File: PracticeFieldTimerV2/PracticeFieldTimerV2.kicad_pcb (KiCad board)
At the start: 2 copper layers, 106 x 153.7 mm, 43 parts, among them J1 External Controls, J3 Panel, J5 /CAN Enable, J6 RJ45-B, J7 RJ45-A, J8 CAN Terminate, U1 ESP32-DevKitC, U2 PCF8574N, U3 20 x 4 LCD, U4 DS3231MZ_TRL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

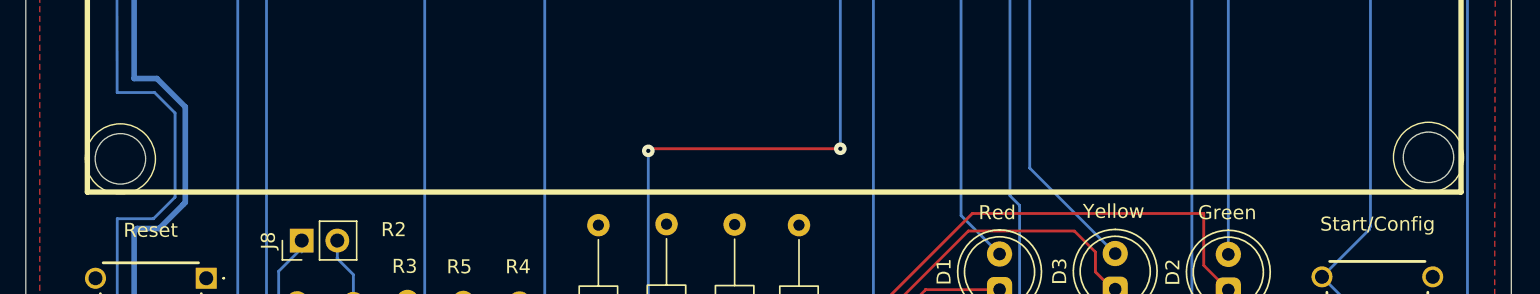
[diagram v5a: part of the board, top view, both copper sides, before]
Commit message: Clean up LCD mounting holes.
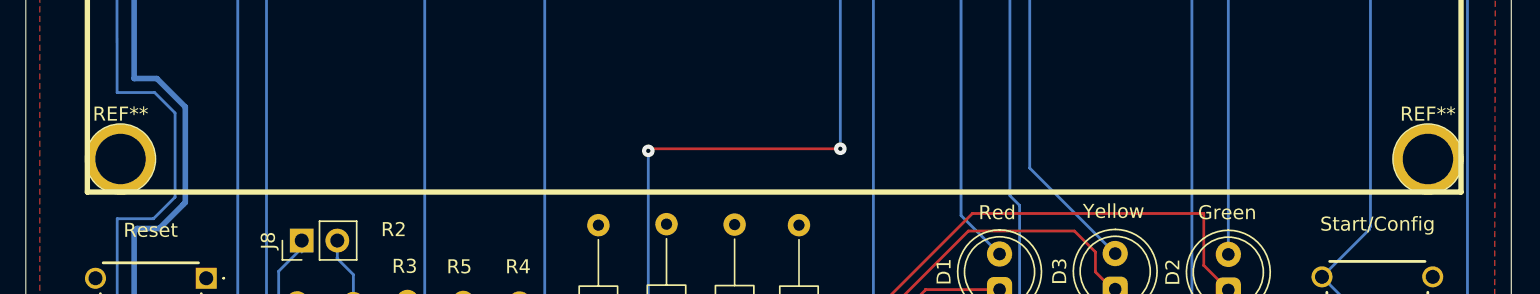
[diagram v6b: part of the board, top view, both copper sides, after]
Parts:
- removed the REF** at (140.1, 119.6)
- removed the REF** at (46.8, 119.7)
- added REF**: Untitled, Misc:M3-Hole-With-2.5mm-Radius-Boundary, F.Cu at (140.0, 119.7)
- added REF**: Untitled, Misc:M3-Hole-With-2.5mm-Radius-Boundary, F.Cu at (46.8, 119.7)
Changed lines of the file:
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@@
 		(embedded_fonts no)
 	)
-	(footprint "Misc:M3_HoleWith2.5mmRing"
-		(layer "F.Cu")
-		(at 140.07 119.57)
-		(property "Reference" "REF**"
-			(at 0 -3.6 0)
-			(unlocked yes)
-			(layer "F.SilkS")
-			(hide yes)
-			(effects
-				(font
-					(size 1 1)
-					(thickness 0.1)
-				)
-			)
-		)
-		(property "Value" "M3_2.5mm_Offset"
-			(at 0 4.2 0)
-			(unlocked yes)
-			(layer "F.Fab")
-			(effects
-				(font
-					(size 1 1)
-					(thickness 0.15)
-				)
-			)
-		)
-		(property "Datasheet" ""
-			(at 0 0 0)
-			(unlocked yes)
-			(layer "F.Fab")
-			(hide yes)
-			(effects
-				(font
-					(size 1 1)
-					(thickness 0.15)
-				)
-			)
-		)
-		(property "Description" "M3 Mounting Hole With 2.5 mm Ring"
-			(at 0 0 0)
-			(unlocked yes)
-			(layer "F.Fab")
-			(hide yes)
-			(effects
-				(font
-					(size 1 1)
-					(thickness 0.15)
-				)
-			)
-		)
-		(attr through_hole)
-		(fp_circle
-			(center 0 0)
-			(end 2.5 0)
-			(stroke
-				(width 0.1)
-				(type solid)
-			)
-			(fill no)
-			(layer "F.SilkS")
-		)
-		(fp_circle
-			(center 0 0)
-			(end 1.8 0)
-			(stroke
-				(width 0.05)
-				(type solid)
-			)
-			(fill no)
-			(layer "Edge.Cuts")
-		)
-		(embedded_fonts no)
-	)
 	(footprint "Misc:SW_500ASSP1M2QE"
 		(locked yes)
@@
 		)
 	)
+	(footprint "Misc:M3-Hole-With-2.5mm-Radius-Boundary"
+		(layer "F.Cu")
+		(at 140.03 119.69)
+		(property "Reference" "REF**"
+			(at 0 -3.2 0)
+			(unlocked yes)
+			(layer "F.SilkS")
+			(effects
+				(font
+					(size 1 1)
+					(thickness 0.1)
+				)
+			)
+		)
+		(property "Value" "Untitled"
+			(at 0 3.3 0)
+			(unlocked yes)
+			(layer "F.Fab")
+			(effects
+				(font
+					(size 1 1)
+					(thickness 0.15)
+				)
+			)
+		)
+		(property "Datasheet" ""
+			(at 0 0 0)
+			(unlocked yes)
+			(layer "F.Fab")
+			(hide yes)
+			(effects
+				(font
+					(size 1 1)
+					(thickness 0.15)
+				)
+			)
+		)
+		(property "Description" ""
+			(at 0 0 0)
+			(unlocked yes)
+			(layer "F.Fab")
+			(hide yes)
+			(effects
+				(font
+					(size 1 1)
+					(thickness 0.15)
+				)
+			)
+		)
+		(attr through_hole)
+		(fp_circle
+			(center 0 0)
+			(end 0 -2.5)
+			(stroke
+				(width 0.1)
+				(type default)
+			)
+			(fill no)
+			(layer "F.SilkS")
+		)
+		(fp_text user "${REFERENCE}"
+			(at 0 4.8 0)
+			(unlocked yes)
+			(layer "F.Fab")
+			(effects
+				(font
+					(size 1 1)
+					(thickness 0.15)
+				)
+			)
+		)
+		(pad "" thru_hole circle
+			(at 0 0)
+			(size 5 5)
+			(drill 3.6)
+			(layers "*.Cu" "*.Mask")
+			(remove_unused_layers no)
+		)
+		(embedded_fonts no)
+	)
 	(footprint "Misc:MountingHole_3.2mm_M3_Pad_TopBottom_Grounded"
 		(locked yes)
@@
 		(embedded_fonts no)
 	)
+	(footprint "Misc:M3-Hole-With-2.5mm-Radius-Boundary"
+		(layer "F.Cu")
+		(at 46.76 119.69)
+		(property "Reference" "REF**"
+			(at 0 -3.2 0)
+			(unlocked yes)
+			(layer "F.SilkS")
+			(effects
+				(font
+					(size 1 1)
+					(thickness 0.1)
+				)
+			)
+		)
+		(property "Value" "Untitled"
+			(at 0 3.3 0)
+			(unlocked yes)
+			(layer "F.Fab")
+			(effects
+				(font
+					(size 1 1)
+					(thickness 0.15)
+				)
+			)
+		)
+		(property "Datasheet" ""
+			(at 0 0 0)
+			(unlocked yes)
+			(layer "F.Fab")
+			(hide yes)
+			(effects
+				(font
+					(size 1 1)
+					(thickness 0.15)
+				)
+			)
+		)
+		(property "Description" ""
+			(at 0 0 0)
+			(unlocked yes)
+			(layer "F.Fab")
+			(hide yes)
+			(effects
+				(font
+					(size 1 1)
+					(thickness 0.15)
+				)
+			)
+		)
+		(attr through_hole)
+		(fp_circle
+			(center 0 0)
+			(end 0 -2.5)
+			(stroke
+				(width 0.1)
+				(type default)
+			)
+			(fill no)
+			(layer "F.SilkS")
+		)
+		(fp_text user "${REFERENCE}"
+			(at 0 4.8 0)
+			(unlocked yes)
+			(layer "F.Fab")
+			(effects
+				(font
+					(size 1 1)
+					(thickness 0.15)
+				)
+			)
+		)
+		(pad "" thru_hole circle
+			(at 0 0)
+			(size 5 5)
+			(drill 3.6)
+			(layers "*.Cu" "*.Mask")
+			(remove_unused_layers no)
+		)
+		(embedded_fonts no)
+	)
 	(footprint "Misc:MountingHole_3.2mm_M3_Pad_TopBottom_Grounded"
 		(locked yes)
@@
 		)
 	)
-	(footprint "Misc:M3_HoleWith2.5mmRing"
-		(layer "F.Cu")
-		(at 46.75 119.68)
-		(property "Reference" "REF**"
-			(at 0 -3.6 0)
-			(unlocked yes)
-			(layer "F.SilkS")
-			(hide yes)
-			(effects
-				(font
-					(size 1 1)
-					(thickness 0.1)
-				)
-			)
-		)
-		(property "Value" "M3_2.5mm_Offset"
-			(at 0 4.2 0)
-			(unlocked yes)
-			(layer "F.Fab")
-			(effects
-				(font
-					(size 1 1)
-					(thickness 0.15)
-				)
-			)
-		)
-		(property "Datasheet" ""
-			(at 0 0 0)
-			(unlocked yes)
-			(layer "F.Fab")
-			(hide yes)
-			(effects
-				(font
-					(size 1 1)
-					(thickness 0.15)
-				)
-			)
-		)
-		(property "Description" "M3 Mounting Hole With 2.5 mm Ring"
-			(at 0 0 0)
-			(unlocked yes)
-			(layer "F.Fab")
-			(hide yes)
-			(effects
-				(font
-					(size 1 1)
-					(thickness 0.15)
-				)
-			)
-		)
-		(attr through_hole)
-		(fp_circle
-			(center 0 0)
-			(end 2.5 0)
-			(stroke
-				(width 0.1)
-				(type solid)
-			)
-			(fill no)
-			(layer "F.SilkS")
-		)
-		(fp_circle
-			(center 0 0)
-			(end 1.8 0)
-			(stroke
-				(width 0.05)
-				(type solid)
-			)
-			(fill no)
-			(layer "Edge.Cuts")
-		)
-		(embedded_fonts no)
-	)
 	(footprint "Resistor_THT:R_Axial_DIN0207_L6.3mm_D2.5mm_P15.24mm_Horizontal"
 		(layer "F.Cu")
@@
 		(min_thickness 0.25)
 		(filled_areas_thickness no)
-		(fill yes
+		(fill
 			(thermal_gap 0.5)
 			(thermal_bridge_width 0.5)

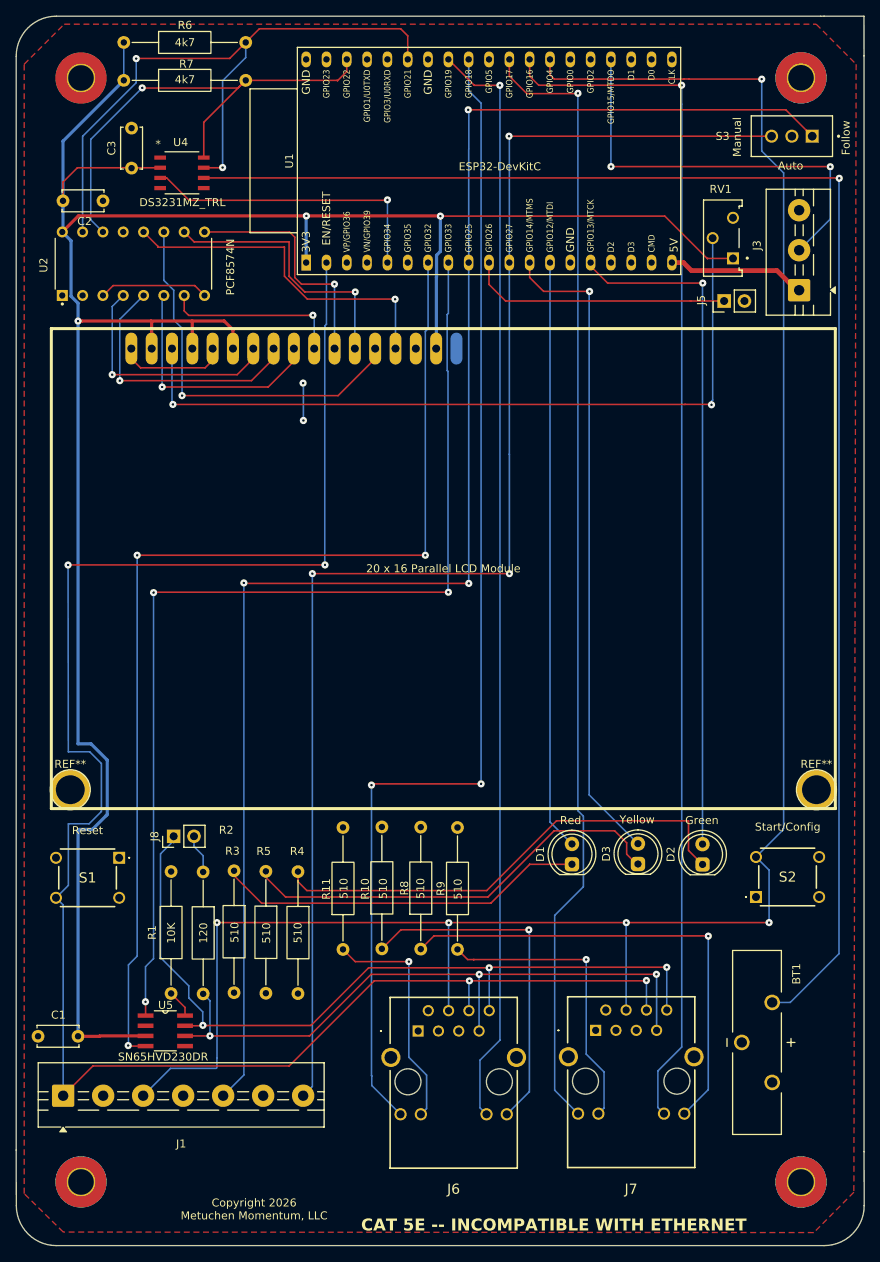
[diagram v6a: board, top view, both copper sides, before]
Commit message: More cleanup: redraw the cut lines to precise dimensions, minor improvements to symbol appearance.
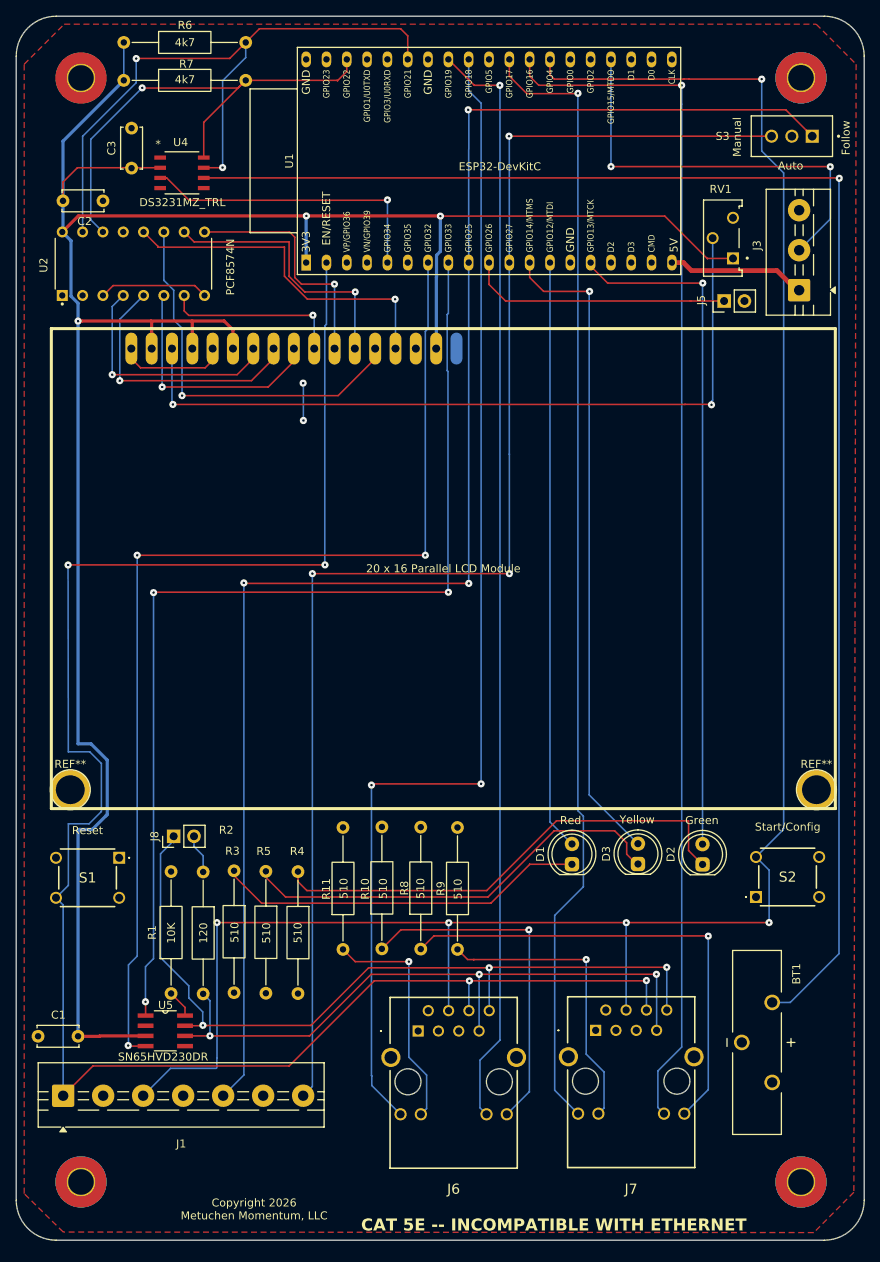
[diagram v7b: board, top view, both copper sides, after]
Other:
- board size 106 x 153.7 mm -> 106 x 153 mm
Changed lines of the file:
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@@
 	)
 	(gr_line
-		(start 141 23)
-		(end 145.97 23)
-		(stroke
-			(width 0.05)
-			(type default)
-		)
-		(layer "Edge.Cuts")
-	)
-	(gr_line
-		(start 145.98 164.935)
-		(end 146 171.675)
-		(stroke
-			(width 0.05)
-			(type default)
-		)
-		(layer "Edge.Cuts")
-	)
-	(gr_arc
-		(start 45.014529 176.675)
-		(mid 41.482704 175.214238)
-		(end 40.01454 171.685482)
+		(start 141 176)
+		(end 45 176)
 		(stroke
 			(width 0.05)
@@
 	)
 	(gr_arc
-		(start 146 171.675)
-		(mid 144.535534 175.210534)
-		(end 141 176.675)
+		(start 40 28)
+		(mid 41.464466 24.464466)
+		(end 45 23)
 		(stroke
 			(width 0.05)
@@
 	)
 	(gr_line
-		(start 145.98 27.96)
-		(end 145.98 164.935)
-		(stroke
-			(width 0.05)
-			(type solid)
-		)
-		(layer "Edge.Cuts")
-	)
-	(gr_line
-		(start 140.56 23)
-		(end 141 23)
+		(start 146 28)
+		(end 146 171)
 		(stroke
 			(width 0.05)
@@
 		(layer "Edge.Cuts")
 	)
-	(gr_line
-		(start 45 23)
-		(end 140.56 23)
+	(gr_arc
+		(start 141 23)
+		(mid 144.535534 24.464466)
+		(end 146 28)
 		(stroke
 			(width 0.05)
@@
 	)
 	(gr_arc
-		(start 40 28)
-		(mid 41.464466 24.464466)
-		(end 45 23)
+		(start 146 171)
+		(mid 144.535534 174.535534)
+		(end 141 176)
 		(stroke
 			(width 0.05)
@@
 	)
 	(gr_line
-		(start 40 164.75)
-		(end 40.01454 171.685482)
+		(start 40 171)
+		(end 40 28)
 		(stroke
 			(width 0.05)
@@
 		(layer "Edge.Cuts")
 	)
-	(gr_line
-		(start 141 176.675)
-		(end 45.014529 176.675)
+	(gr_arc
+		(start 45 176)
+		(mid 41.464466 174.535534)
+		(end 40 171)
 		(stroke
 			(width 0.05)
@@
 	)
 	(gr_line
-		(start 40 164.75)
-		(end 40 28)
+		(start 45 23)
+		(end 141 23)
 		(stroke
 			(width 0.05)
@@
 	)
 	(gr_line
-		(start 145.97 23)
-		(end 145.98 27.96)
-		(stroke
-			(width 0.05)
-			(type solid)
-		)
-		(layer "Edge.Cuts")
-	)
-	(gr_line
 		(start 65.97 125.56)
 		(end 64.31 128.87)
@@
 		(min_thickness 0.25)
 		(filled_areas_thickness no)
-		(fill
+		(fill yes
 			(thermal_gap 0.5)
 			(thermal_bridge_width 0.5)

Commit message: Fix egregious wiring error in the LCD Display
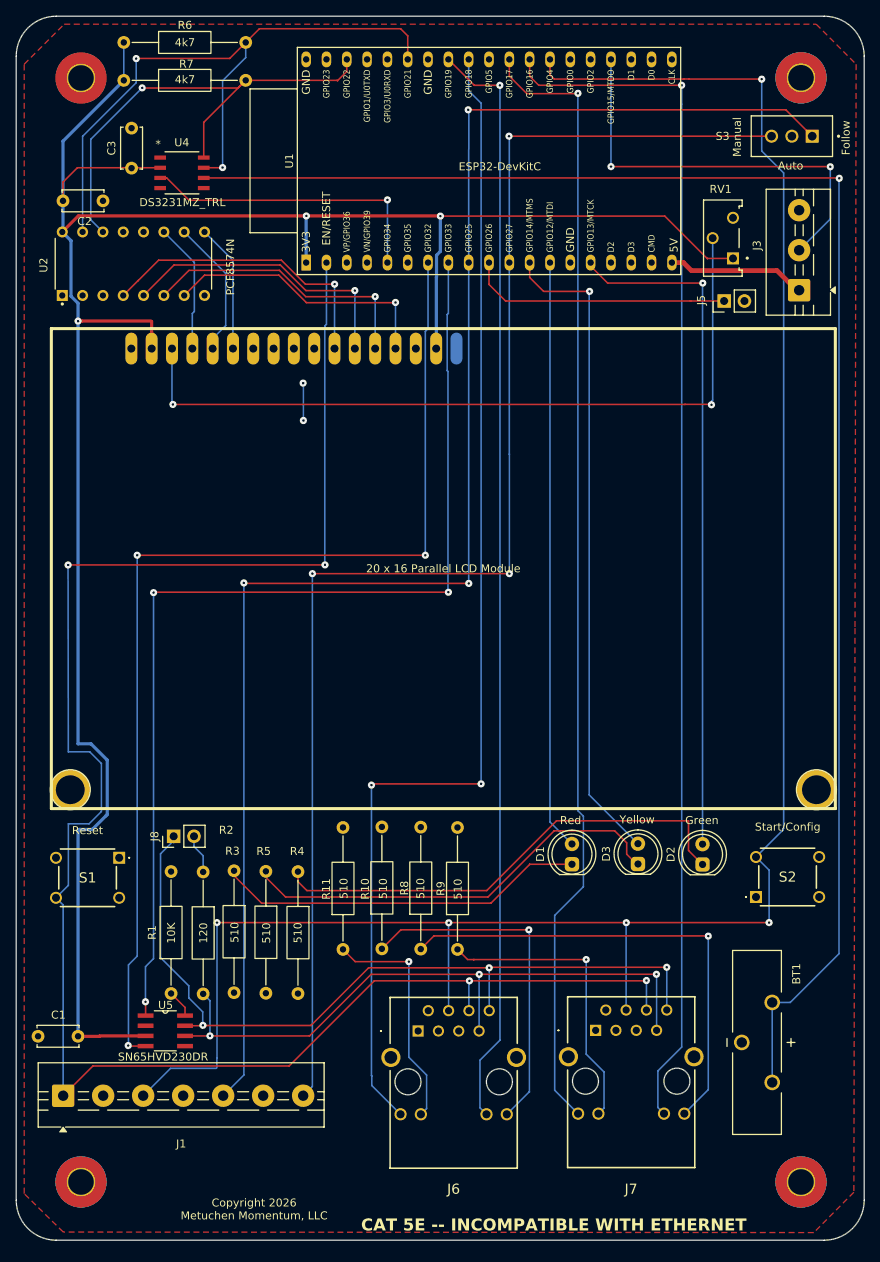
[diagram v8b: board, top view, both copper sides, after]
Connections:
- BT1 pad P_2: (no net) -> Net-(U4-VBAT)
- REF** pad : (no net) -> GND (x2)
- U2 pad 12: Net-(U2-P7) -> unconnected-(U2-P7-Pad12)
- U3 pad 10: Net-(U2-P3) -> unconnected-(U3-DB3-Pad10)
- U3 pad 11: Net-(U2-P4) -> Net-(U2-P0)
- U3 pad 12: Net-(U2-P5) -> Net-(U2-P1)
- U3 pad 13: Net-(U2-P6) -> Net-(U2-P2)
- U3 pad 14: Net-(U2-P7) -> Net-(U2-P3)
- U3 pad 4: +3.3V -> Net-(U2-P6)
- U3 pad 5: GND -> Net-(U2-P5)
- U3 pad 6: +3.3V -> Net-(U2-P4)
- U3 pad 7: Net-(U2-P0) -> unconnected-(U3-DB0-Pad7)
- U3 pad 8: Net-(U2-P1) -> unconnected-(U3-DB1-Pad8)
- U3 pad 9: Net-(U2-P2) -> unconnected-(U3-DB2-Pad9)
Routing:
- net Net-(U2-P7): track 43.3 -> 0.00 mm, vias 1 -> 0
- net Net-(U2-P6): track 48.9 -> 16.3 mm, vias 1 -> 0
- net GND: track 32.2 -> 6.06 mm
- net +3.3V: track 298.6 -> 282.1 mm
- net Net-(U2-P5): track 34.1 -> 18.9 mm, vias 1 -> 0
- net Net-(U2-P4): track 30.0 -> 16.0 mm, vias 1 -> 0
- net Net-(U2-P3): track 23.0 -> 34.7 mm
- net Net-(U4-VBAT): track 187.3 -> 197.3 mm
- net Net-(U2-P0): track 30.3 -> 37.6 mm
- net Net-(U2-P2): track 31.4 -> 37.7 mm
- net Net-(U2-P1): track 33.5 -> 36.2 mm
- net unconnected-(U3-DB2-Pad9): track 0.00 -> 1.59 mm
- net unconnected-(U3-DB0-Pad7): track 0.00 -> 1.35 mm
- net unconnected-(U3-DB1-Pad8): track 0.00 -> 1.25 mm
